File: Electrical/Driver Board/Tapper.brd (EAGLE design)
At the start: 69.6 x 28.6 mm, 38 parts, among them M0 B2B-PH-K, M1 B2B-PH-K, M2 B2B-PH-K, M3 B2B-PH-K, M4 B2B-PH-K, M5 B2B-PH-K, M6 B2B-PH-K, M7 B2B-PH-K, P1 B5B-PH-K, P2 B4B-PH-K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

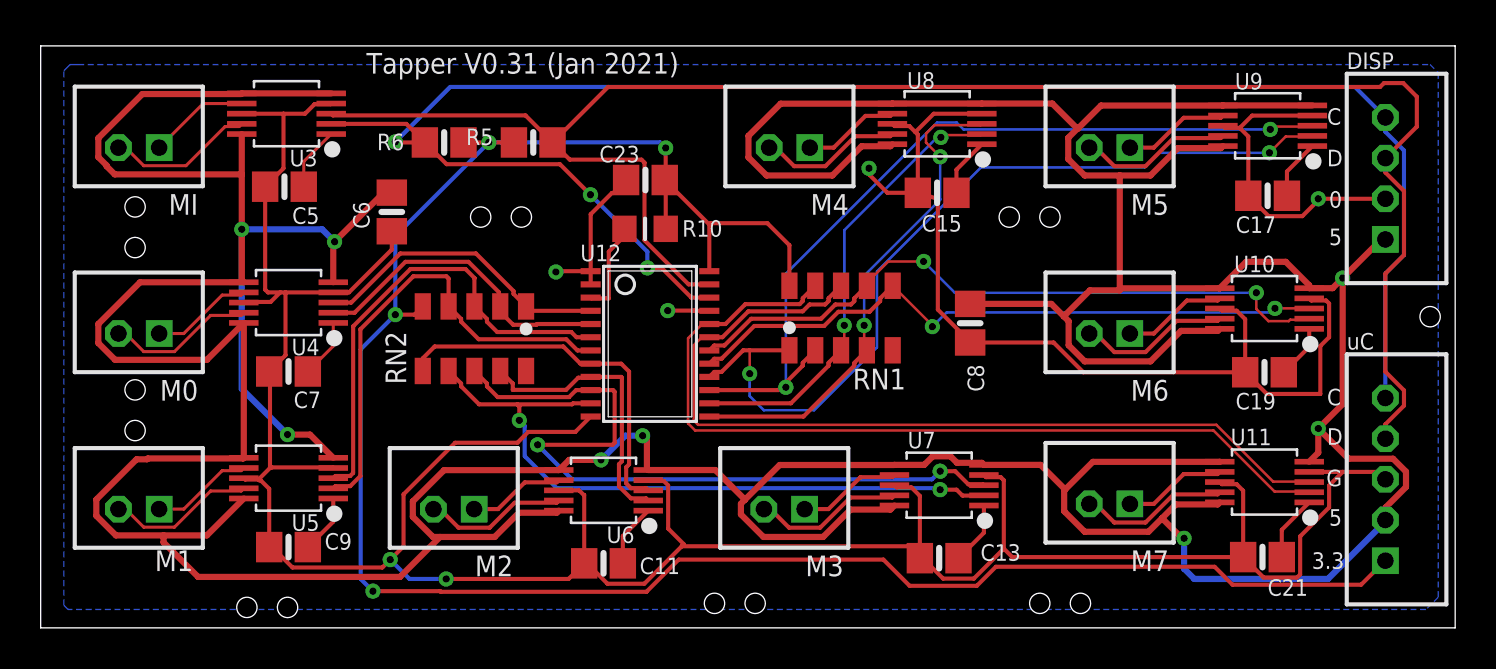
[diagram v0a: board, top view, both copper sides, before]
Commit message: 0.32: Add 3v3 reg, remove disp, add buffer for (hopefully) enabling the lone driver
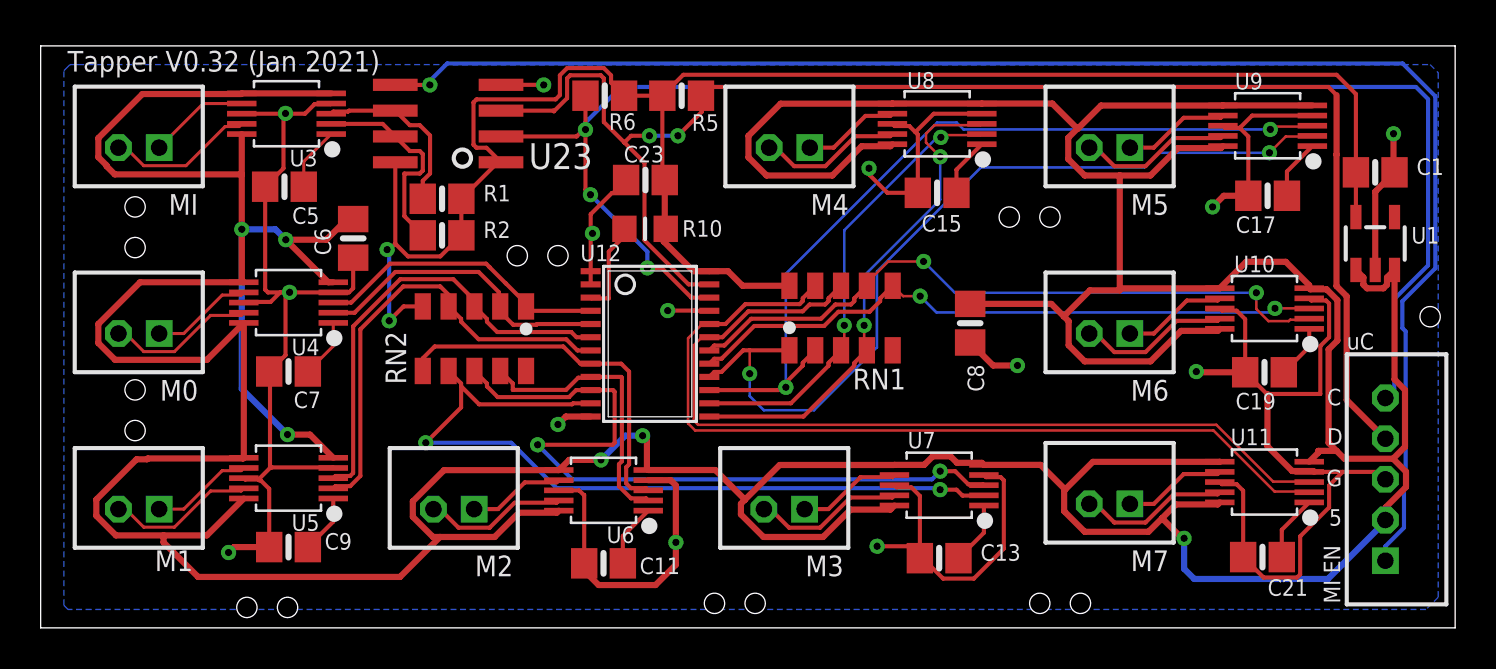
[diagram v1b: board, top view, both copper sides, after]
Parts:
- removed P2: B4B-PH-K, con-jst-ph:B4B-PH-K
- added C1: 1uF, microbuilder:0805-NO
- added R1, R2: 10K, microbuilder:0805-NO
- added U1: TLV743P, microbuilder:SOT23-5
- added U23: PCA9515B, PCA9517:SO-08
- moved R6 8.23 mm to (18.6, 29.0)
- moved R5 7.65 mm to (22.4, 29.0)
- moved C6 2.30 mm to (6.23, 22.0)
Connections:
- new net N$12: R1.1, U23.6, U3.3
- new net N$13: R2.1, U23.7, U3.2
- new net N$5: P1.1, U23.5
- net +5V: now also U1.1, U1.3; no longer P2.1
- net GND: now also C1.2, U1.2, U23.4; no longer P2.2
- net INPUTSCL: now also U23.2; no longer P2.4, U3.2
- net INPUTSDA: now also U23.3; no longer P2.3, U3.3
- net VIN: now also C1.1, R1.2, R2.2, U1.5, U23.1, U23.8; no longer P1.1
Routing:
- net N$5: track 0.00 -> 76.4 mm, vias 0 -> 1
- net GND: track 216.1 -> 156.1 mm, vias 6 -> 14
- net VIN: track 105.8 -> 88.9 mm, vias 4 -> 2
- net INPUTSDA: track 87.3 -> 74.1 mm, vias 0 -> 2
- net INPUTSCL: track 89.1 -> 76.1 mm
- net N$13: track 0.00 -> 10.3 mm
- net N$12: track 0.00 -> 8.69 mm
- net +5V: track 302.3 -> 308.9 mm, vias 8 -> 6
- net 3SCL: track 33.9 -> 39.8 mm
- net 1SDA: track 23.4 -> 22.4 mm
- net 1SCL: track 23.6 -> 22.7 mm
- net 6SDA: track 32.4 -> 31.8 mm
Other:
- board text added: "MI EN"
- board text added: "Tapper V0.32 (Jan 2021)"
- board text removed: "0"
- board text removed: "3.3"
- board text removed: "DISP"
- board text removed: "Tapper V0.31 (Jan 2021)"

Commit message: Add power led
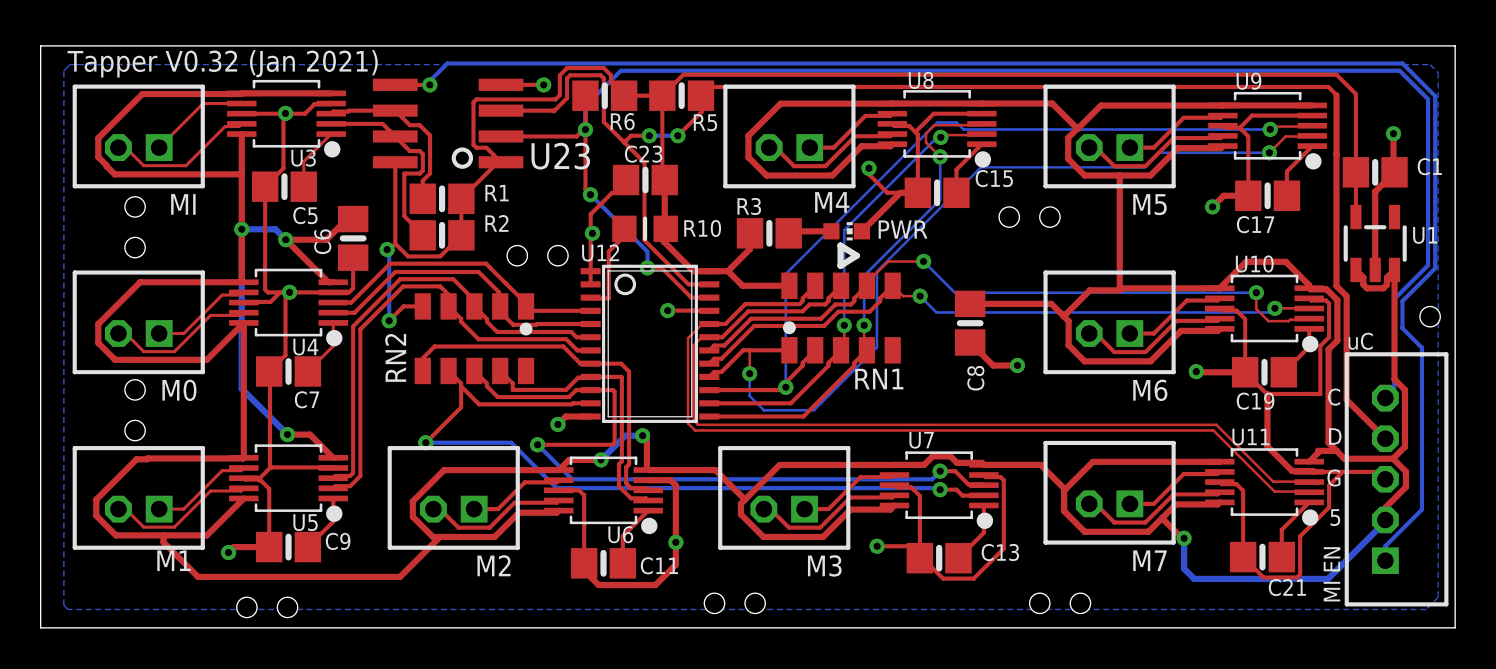
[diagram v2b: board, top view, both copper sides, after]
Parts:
- added PWR: EL-19-21VGC/TR8, adafruit:CHIP-LED0603
- added R3: 100, microbuilder:0805-NO
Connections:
- new net N$14: PWR.A, R3.1
- net GND: now also PWR.C
- net VIN: now also R3.2
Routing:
- net GND: track 156.1 -> 159.6 mm
- net VIN: track 88.9 -> 91.2 mm
- net N$14: track 0.00 -> 2.14 mm
- net INPUTSCL: track 76.1 -> 77.2 mm
- net N$5: track 76.4 -> 77.0 mm
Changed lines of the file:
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@@
 <text x="55.102" y="16.484" size="0.8128" layer="25">uC</text>
 <circle x="11.6" y="25.9" radius="0.4242625" width="0.2032" layer="25"/>
+<wire x1="30.2" y1="21.6" x2="30.2" y2="20.6" width="0.3048" layer="25"/>
+<wire x1="30.2" y1="20.6" x2="31" y2="21.1" width="0.3048" layer="25"/>
+<wire x1="31" y1="21.1" x2="30.2" y2="21.6" width="0.3048" layer="25"/>
 </plain>
 <attributes>
@@
 </element>
 <element name="C15" library="microbuilder" package="0805-NO" value="1uF" x="34.952" y="24.194" smashed="yes">
-<attribute name="NAME" x="34.19" y="22.289" size="0.8128" layer="25" ratio="18"/>
+<attribute name="NAME" x="36.79" y="24.489" size="0.8128" layer="25" ratio="18"/>
 </element>
 <element name="C17" library="microbuilder" package="0805-NO" value="1uF" x="51.208" y="24.048" smashed="yes">
@@
 <element name="M4" library="con-jst-ph" package="B2B-PH-K" value="B2B-PH-K" x="27.686" y="26.416" smashed="yes" rot="R180">
 <attribute name="LABEL" value="" x="30.607" y="30.861" size="1.016" layer="25" ratio="18" rot="R180"/>
-<attribute name="NAME" x="30.607" y="24.13" size="1.016" layer="25" ratio="18" rot="R180"/>
+<attribute name="NAME" x="30.707" y="24.23" size="1.016" layer="25" ratio="18" rot="R180"/>
 </element>
 <element name="P1" library="con-jst-ph" package="B5B-PH-K" value="B5B-PH-K" x="57" y="10.1" smashed="yes" rot="R90">
@@
 </element>
 <element name="R2" library="microbuilder" package="0805-NO" value="10K" x="10.6" y="22.1" smashed="yes">
-<attribute name="NAME" x="12.632" y="21.973" size="0.8128" layer="25" ratio="18"/>
+<attribute name="NAME" x="12.632" y="22.273" size="0.8128" layer="25" ratio="18"/>
+</element>
+<element name="PWR" library="adafruit" library_urn="urn:adsk.eagle:library:420" package="CHIP-LED0603" package3d_urn="urn:adsk.eagle:package:6240556/1" value="EL-19-21VGC/TR8" x="30.5" y="22.3" smashed="yes" rot="R270">
+<attribute name="NAME" x="31.965" y="21.935" size="0.9" layer="25"/>
+</element>
+<element name="R3" library="microbuilder" package="0805-NO" value="100" x="26.7" y="22.2" smashed="yes" rot="R180">
+<attribute name="NAME" x="26.368" y="23.927" size="0.8128" layer="25" ratio="18" rot="R180"/>
 </element>
 </elements>
@@
 <wire x1="22.466" y1="30" x2="54.6029" y2="30" width="0.2032" layer="1"/>
 <wire x1="55.55" y1="25.2" x2="55.55" y2="23.0001" width="0.2032" layer="1"/>
+<contactref element="R3" pad="2"/>
+<wire x1="25.75" y1="22.2" x2="25.75" y2="21.428" width="0.3048" layer="1"/>
+<wire x1="25.75" y1="21.428" x2="24.661" y2="20.339" width="0.3048" layer="1"/>
 </signal>
 <signal name="GND" class="1">
@@
 <wire x1="18.3" y1="4.9" x2="17.412" y2="5.788" width="0.3048" layer="1"/>
 <via x="22.1" y="7" extent="1-16" drill="0.35"/>
+<contactref element="PWR" pad="C"/>
+<wire x1="31.25" y1="22.3" x2="33.144" y2="24.194" width="0.3048" layer="1"/>
+<wire x1="33.144" y1="24.194" x2="34.002" y2="24.194" width="0.3048" layer="1"/>
 </signal>
 <signal name="N$2">
@@
 <wire x1="22.861" y1="19.039" x2="21.4" y2="20.5" width="0.2032" layer="1"/>
 <wire x1="22.861" y1="19.039" x2="23.7458" y2="19.039" width="0.2032" layer="1"/>
-<wire x1="58.5" y1="29.4" x2="19.4" y2="29.4" width="0.2032" layer="16"/>
+<wire x1="57.7" y1="30.2" x2="19.4" y2="30.2" width="0.2032" layer="16"/>
 <contactref element="P1" pad="5"/>
 <contactref element="U23" pad="2"/>
@@
 <wire x1="17.654" y1="27.4" x2="17.654" y2="27.3" width="0.2032" layer="1"/>
 <wire x1="17.654" y1="27.3" x2="17.654" y2="24.346" width="0.2032" layer="1"/>
-<wire x1="58.5" y1="29.4" x2="59.1" y2="28.8" width="0.2032" layer="16"/>
+<wire x1="57.7" y1="30.2" x2="59.1" y2="28.8" width="0.2032" layer="16"/>
 <wire x1="59.1" y1="28.8" x2="59.1" y2="20.628425" width="0.2032" layer="16"/>
 <wire x1="59.1" y1="20.628425" x2="57.4364" y2="18.964825" width="0.2032" layer="16"/>
@@
 <wire x1="13.5" y1="26.965" x2="17.219" y2="26.965" width="0.2032" layer="1"/>
 <wire x1="17.219" y1="26.965" x2="17.654" y2="27.4" width="0.2032" layer="1"/>
-<wire x1="19.4" y1="29.4" x2="17.654" y2="27.654" width="0.2032" layer="16"/>
-<wire x1="17.654" y1="27.654" x2="17.654" y2="27.3" width="0.2032" layer="16"/>
+<wire x1="19.4" y1="30.2" x2="17.654" y2="28.454" width="0.2032" layer="16"/>
+<wire x1="17.654" y1="28.454" x2="17.654" y2="27.3" width="0.2032" layer="16"/>
 <via x="17.654" y="27.3" extent="1-16" drill="0.35"/>
 </signal>
@@
 <contactref element="U23" pad="5"/>
 <wire x1="57" y1="6.1" x2="57" y2="6.8068375" width="0.2032" layer="16"/>
-<wire x1="58" y1="9.7" x2="57.9144" y2="9.6144" width="0.2032" layer="16"/>
-<wire x1="57" y1="6.8068375" x2="57.9144" y2="7.7212375" width="0.2032" layer="16"/>
-<wire x1="57.9144" y1="7.7212375" x2="57.9144" y2="9.6144" width="0.2032" layer="16"/>
-<wire x1="57.8364" y1="17.535175" x2="58" y2="17.371575" width="0.2032" layer="16"/>
+<wire x1="57" y1="6.8068375" x2="58.8" y2="8.6068375" width="0.2032" layer="16"/>
+<wire x1="58.8" y1="8.6068375" x2="58.8" y2="16.571575" width="0.2032" layer="16"/>
+<wire x1="57.8364" y1="17.535175" x2="58.8" y2="16.571575" width="0.2032" layer="16"/>
 <wire x1="59.4556" y1="20.481125" x2="57.8364" y2="18.861925" width="0.2032" layer="16"/>
 <wire x1="59.4556" y1="20.481125" x2="59.4556" y2="28.9473" width="0.2032" layer="16"/>
@@
 <wire x1="8.305" y1="29.5" x2="8.3" y2="29.505" width="0.2032" layer="1"/>
 <wire x1="57.8364" y1="18.861925" x2="57.8364" y2="17.535175" width="0.2032" layer="16"/>
-<wire x1="58" y1="17.371575" x2="58" y2="9.7" width="0.2032" layer="16"/>
 </signal>
 <signal name="N$12">
@@
 <wire x1="8.746" y1="23.0447875" x2="8.746" y2="25.141" width="0.2032" layer="1"/>
 </signal>
+<signal name="N$14">
+<contactref element="R3" pad="1"/>
+<contactref element="PWR" pad="A"/>
+<wire x1="29.75" y1="22.3" x2="27.75" y2="22.3" width="0.3048" layer="1"/>
+<wire x1="27.65" y1="22.2" x2="27.75" y2="22.3" width="0.3048" layer="1"/>
+</signal>
 </signals>
 <mfgpreviewcolors>
@@
 </board>
 </drawing>
+<compatibility>
+<note version="8.2" severity="warning">
+Since Version 8.2, EAGLE supports online libraries. The ids
+of those online libraries will not be understood (or retained)
+with this version.
+</note>
+<note version="8.3" severity="warning">
+Since Version 8.3, EAGLE supports URNs for individual library
+assets (packages, symbols, and devices). The URNs of those assets
+will not be understood (or retained) with this version.
+</note>
+<note version="8.3" severity="warning">
+Since Version 8.3, EAGLE supports the association of 3D packages
+with devices in libraries, schematics, and board files. Those 3D
+packages will not be understood (or retained) with this version.
+</note>
+</compatibility>
 </eagle>
